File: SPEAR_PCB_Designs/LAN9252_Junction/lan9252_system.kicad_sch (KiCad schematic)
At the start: 32 parts, among them SW2 SW_MEC_5E, U1 LAN9252_ML, Y1 25MHz

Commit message: Almost finished board
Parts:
- removed C1, C3: 1uF, Capacitor_SMD:C_0201_0603Metric, symbol Device:C
- removed C11, C22, C8: 0.1uF, Capacitor_SMD:C_0201_0603Metric, symbol Device:C
- removed R2: 10k, Resistor_SMD:R_0603_1608Metric, symbol Device:R_US
- added C66: 0.1uF, Capacitor_SMD:C_0201_0603Metric, symbol Device:C
- added R5, R6: 141 R, Resistor_SMD:R_0402_1005Metric, symbol Device:R_US
- added R57: 10k, Resistor_SMD:R_0402_1005Metric, symbol Device:R_US
- C1: renamed from C6; footprint Capacitor_SMD:C_0201_0603Metric -> Capacitor_SMD:C_0402_1005Metric
- C10: renamed from C20; value 0.1uF -> 470 pF; footprint Capacitor_SMD:C_0201_0603Metric -> Capacitor_SMD:C_0402_1005Metric
- C11: renamed from C12; footprint Capacitor_SMD:C_0201_0603Metric -> Capacitor_SMD:C_0402_1005Metric
- C12: renamed from C21; footprint Capacitor_SMD:C_0201_0603Metric -> Capacitor_SMD:C_0402_1005Metric
- C13, C14, C15, C16, C17, C2, C5: footprint Capacitor_SMD:C_0201_0603Metric -> Capacitor_SMD:C_0402_1005Metric
- C3: renamed from C4; footprint Capacitor_SMD:C_0201_0603Metric -> Capacitor_SMD:C_0402_1005Metric
- C4: renamed from C7; footprint Capacitor_SMD:C_0201_0603Metric -> Capacitor_SMD:C_0402_1005Metric
- C6: renamed from C9; footprint Capacitor_SMD:C_0201_0603Metric -> Capacitor_SMD:C_0402_1005Metric
- C7: renamed from C18; value 0.1uF -> 1uF; footprint Capacitor_SMD:C_0201_0603Metric -> Capacitor_SMD:C_0402_1005Metric
- C8: renamed from C10; footprint Capacitor_SMD:C_0201_0603Metric -> Capacitor_SMD:C_0402_1005Metric
- C9: renamed from C19; footprint Capacitor_SMD:C_0201_0603Metric -> Capacitor_SMD:C_0402_1005Metric
- FB1, FB2, FB3, FB4: footprint Footprints SPEAR:Ferrite_bead -> SPEAR_FOOTPRINTS:Ferrite_bead
- R3: renamed from R25; footprint Resistor_SMD:R_0603_1608Metric -> Resistor_SMD:R_0402_1005Metric
- R4: renamed from R1; footprint Resistor_SMD:R_0603_1608Metric -> Resistor_SMD:R_0402_1005Metric
- U1: footprint Footprints SPEAR:QFP50P1200X1200X120-65N -> SPEAR_FOOTPRINTS:LAN9252_QFN UPDATED
- Y1: footprint Crystal:Crystal_HC50_Vertical -> SPEAR_FOOTPRINTS:Y_Wurth_WE-XTAL_Quartz-HC49-4HSMX
- renumbered SW2 to SW1
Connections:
- net GNDREF is gone; now on net GND: C1.1, C10.2, C11.2, C12.2, C13.2, C14.2, C15.2, C16.2, C17.2, C4.1, C6.2, C7.2, C8.2, C9.2, R4.1, SW1.1, SW1.2, U1.4 (OSCVSS), U1.41 (TESTMODE), U1.65 (VSS), U1.8 (~{FXLOSEN}), U1.9 (FXSDA/FXLOSA/~{FXSDENA})
- net +3.3V: now also R57.1; no longer C5.1
- net GND: now also C2.2, C3.2, U1.10 (FXSDB/FXLOSB/~{FXSDENB}), C66.2, R5.2, R6.2
- net MII_TXD2: now also R5.1
- net MII_TXD3: now also R6.1
- net at FB3.1, U1.58 (VDD33BIAS): now also C5.1
- net TP3 renamed TP1
- net TP1: now also C66.1, R57.2
- no-connect marks 11 -> 10
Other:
- note added: "TX SHIFT STRAP"
- moved on the sheet: C4, C5, FB3, SW1

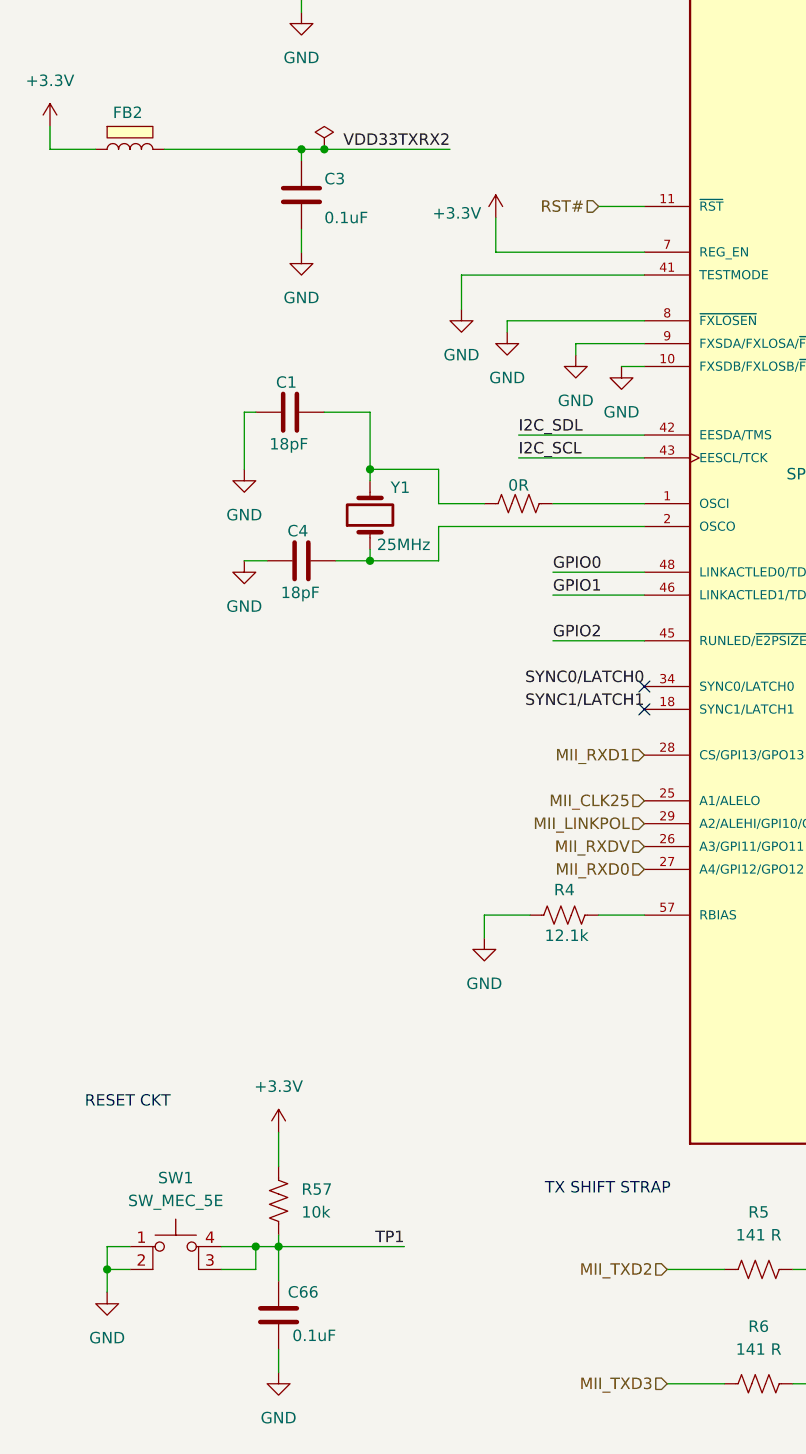
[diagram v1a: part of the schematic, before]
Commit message: Updated Junction board
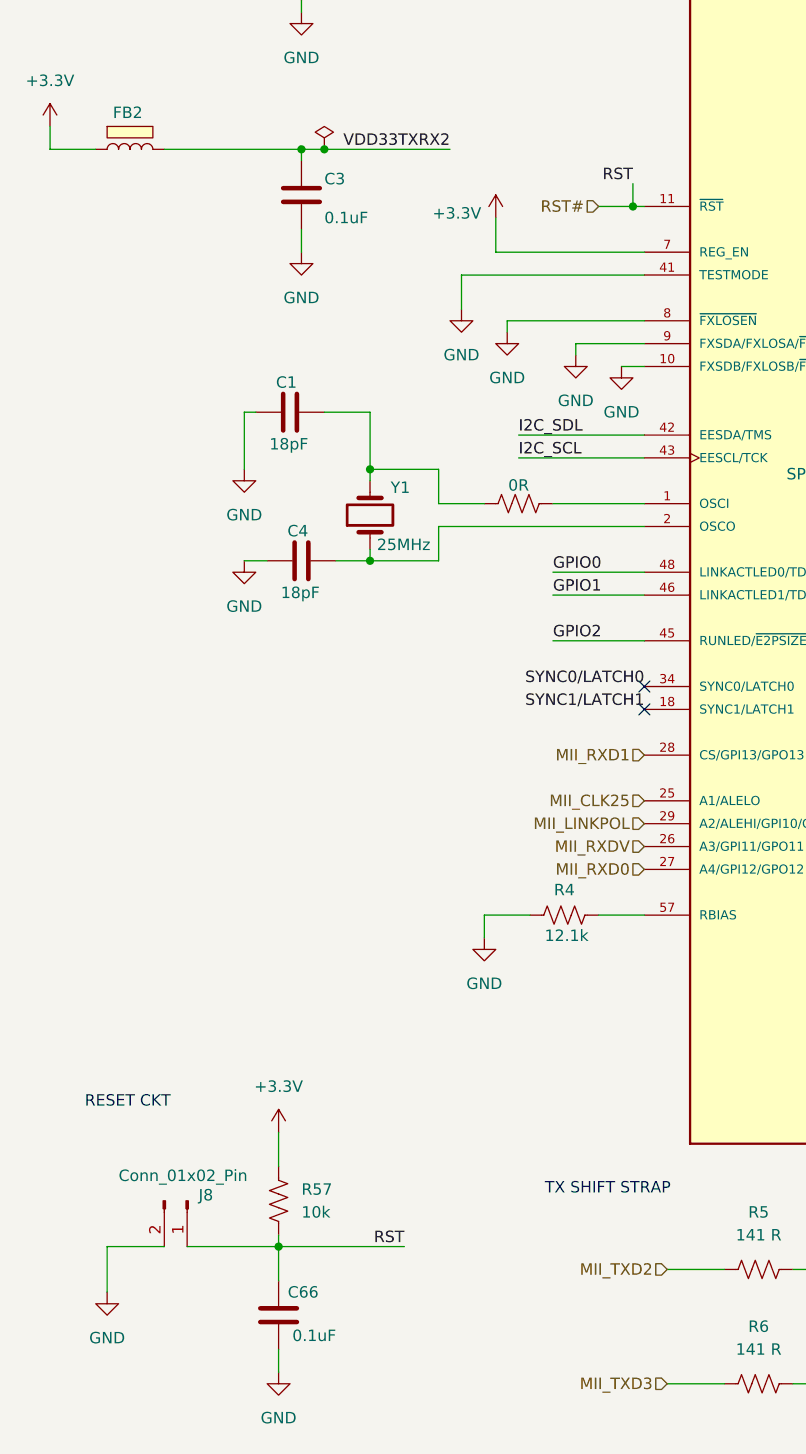
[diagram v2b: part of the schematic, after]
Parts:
- removed SW1: SW_MEC_5E, Button_Switch_THT:SW_PUSH_6mm, symbol Switch:SW_MEC_5E
- added J8: Conn_01x02_Pin, TestPoint:TestPoint_2Pads_Pitch2.54mm_Drill0.8mm, symbol Connector:Conn_01x02_Pin
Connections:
- net TP1 is gone; now on net RST#: C66.1, R57.2
- net GND: now also J8.2 (Pin_2)
- net RST#: now also J8.1 (Pin_1)
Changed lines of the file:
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@@
 	)
 	(junction
+		(at 83.82 55.88)
+		(diameter 0)
+		(color 0 0 0 0)
+	)
+	(junction
 		(at 160.02 35.56)
 		(diameter 0)
@@
 	)
 	(junction
-		(at 25.4 173.99)
-		(diameter 0)
-		(color 0 0 0 0)
-	)
-	(junction
 		(at 237.49 104.14)
 		(diameter 0)
@@
 	)
 	(junction
-		(at 41.91 171.45)
-		(diameter 0)
-		(color 0 0 0 0)
-	)
-	(junction
 		(at 223.52 72.39)
 		(diameter 0)
@@
 	(wire
 		(pts
+			(xy 83.82 53.34) (xy 83.82 55.88)
+		)
+		(stroke
+			(width 0)
+			(type default)
+		)
+	)
+	(wire
+		(pts
 			(xy 237.49 99.06) (xy 237.49 104.14)
 		)
@@
 	(wire
 		(pts
+			(xy 34.29 171.45) (xy 44.45 171.45)
+		)
+		(stroke
+			(width 0)
+			(type default)
+		)
+	)
+	(wire
+		(pts
 			(xy 62.23 88.9) (xy 62.23 85.09)
 		)
@@
 	(wire
 		(pts
-			(xy 27.94 173.99) (xy 25.4 173.99)
-		)
-		(stroke
-			(width 0)
-			(type default)
-		)
-	)
-	(wire
-		(pts
 			(xy 40.64 78.74) (xy 41.91 78.74)
 		)
@@
 	(wire
 		(pts
-			(xy 160.02 43.18) (xy 156.21 43.18)
+			(xy 83.82 55.88) (xy 85.09 55.88)
 		)
 		(stroke
@@
 	(wire
 		(pts
-			(xy 49.53 24.13) (xy 63.5 24.13)
+			(xy 160.02 43.18) (xy 156.21 43.18)
 		)
 		(stroke
@@
 	(wire
 		(pts
-			(xy 25.4 173.99) (xy 25.4 176.53)
+			(xy 49.53 24.13) (xy 63.5 24.13)
 		)
 		(stroke
@@
 	(wire
 		(pts
-			(xy 25.4 173.99) (xy 25.4 171.45)
+			(xy 25.4 171.45) (xy 25.4 176.53)
 		)
 		(stroke
@@
 	(wire
 		(pts
-			(xy 27.94 171.45) (xy 25.4 171.45)
+			(xy 25.4 171.45) (xy 31.75 171.45)
 		)
 		(stroke
@@
 	(wire
 		(pts
-			(xy 41.91 171.45) (xy 44.45 171.45)
-		)
-		(stroke
-			(width 0)
-			(type default)
-		)
-	)
-	(wire
-		(pts
-			(xy 80.01 55.88) (xy 85.09 55.88)
+			(xy 80.01 55.88) (xy 83.82 55.88)
 		)
 		(stroke
@@
 	(wire
 		(pts
-			(xy 41.91 173.99) (xy 41.91 171.45)
-		)
-		(stroke
-			(width 0)
-			(type default)
-		)
-	)
-	(wire
-		(pts
-			(xy 38.1 171.45) (xy 41.91 171.45)
-		)
-		(stroke
-			(width 0)
-			(type default)
-		)
-	)
-	(wire
-		(pts
 			(xy 156.21 78.74) (xy 166.37 78.74)
 		)
@@
 	(wire
 		(pts
-			(xy 38.1 173.99) (xy 41.91 173.99)
-		)
-		(stroke
-			(width 0)
-			(type default)
-		)
-	)
-	(wire
-		(pts
 			(xy 213.36 142.24) (xy 226.06 142.24)
 		)
@@
 		)
 	)
-	(label "TP1"
+	(label "RST"
 		(at 58.42 171.45 180)
 		(effects
@@
 		)
 	)
+	(label "RST"
+		(at 83.82 53.34 180)
+		(effects
+			(font
+				(size 1.27 1.27)
+			)
+			(justify right bottom)
+		)
+	)
 	(label "VDDCR"
 		(at 162.56 43.18 180)
@@
 	)
 	(symbol
+		(lib_id "Connector:Conn_01x02_Pin")
+		(at 34.29 166.37 270)
+		(unit 1)
+		(exclude_from_sim no)
+		(in_bom yes)
+		(on_board yes)
+		(dnp no)
+		(property "Reference" "J8"
+			(at 35.56 165.7349 90)
+			(effects
+				(font
+					(size 1.27 1.27)
+				)
+				(justify left)
+			)
+		)
+		(property "Value" "Conn_01x02_Pin"
+			(at 26.67 163.576 90)
+			(effects
+				(font
+					(size 1.27 1.27)
+				)
+				(justify left)
+			)
+		)
+		(property "Footprint" "TestPoint:TestPoint_2Pads_Pitch2.54mm_Drill0.8mm"
+			(at 34.29 166.37 0)
+			(effects
+				(font
+					(size 1.27 1.27)
+				)
+				(hide yes)
+			)
+		)
+		(property "Datasheet" "~"
+			(at 34.29 166.37 0)
+			(effects
+				(font
+					(size 1.27 1.27)
+				)
+				(hide yes)
+			)
+		)
+		(property "Description" "Generic connector, single row, 01x02, script generated"
+			(at 34.29 166.37 0)
+			(effects
+				(font
+					(size 1.27 1.27)
+				)
+				(hide yes)
+			)
+		)
+		(pin "1"
+		)
+		(pin "2"
+		)
+		(instances
+			(project ""
+				(path "/16d72164-3a84-4f74-a868-383d0ad57128/51ada2c8-3854-4465-9d64-3e8aa0c5daf2"
+					(reference "J8")
+					(unit 1)
+				)
+				(path "/16d72164-3a84-4f74-a868-383d0ad57128/52e6a653-4436-4d7a-ae83-cfeea5b0a028"
+					(reference "J9")
+					(unit 1)
+				)
+			)
+		)
+	)
+	(symbol
 		(lib_id "Device:FerriteBead")
 		(at 241.3 21.59 0)
@@
 					(unit 1)
 				)
-			)
-		)
-	)
-	(symbol
-		(lib_id "Switch:SW_MEC_5E")
-		(at 33.02 173.99 0)
-		(unit 1)
-		(exclude_from_sim no)
-		(in_bom yes)
-		(on_board yes)
-		(dnp no)
-		(fields_autoplaced yes)
-		(property "Reference" "SW1"
-			(at 33.02 163.83 0)
-			(effects
-				(font
-					(size 1.27 1.27)
-				)
-			)
-		)
-		(property "Value" "SW_MEC_5E"
-			(at 33.02 166.37 0)
-			(effects
-				(font
-					(size 1.27 1.27)
-				)
-			)
-		)
-		(property "Footprint" "Button_Switch_THT:SW_PUSH_6mm"
-			(at 33.02 166.37 0)
-			(effects
-				(font
-					(size 1.27 1.27)
-				)
-				(hide yes)
-			)
-		)
-		(property "Datasheet" "http://www.apem.com/int/index.php?controller=attachment&id_attachment=1371"
-			(at 33.02 166.37 0)
-			(effects
-				(font
-					(size 1.27 1.27)
-				)
-				(hide yes)
-			)
-		)
-		(property "Description" "MEC 5E single pole normally-open tactile switch"
-			(at 33.02 173.99 0)
-			(effects
-				(font
-					(size 1.27 1.27)
-				)
-				(hide yes)
-			)
-		)
-		(pin "1"
-		)
-		(pin "3"
-		)
-		(pin "4"
-		)
-		(pin "2"
-		)
-		(instances
-			(project "LAN9252_Junction"
-				(path "/16d72164-3a84-4f74-a868-383d0ad57128/51ada2c8-3854-4465-9d64-3e8aa0c5daf2"
-					(reference "SW1")
-					(unit 1)
-				)
-				(path "/16d72164-3a84-4f74-a868-383d0ad57128/52e6a653-4436-4d7a-ae83-cfeea5b0a028"
-					(reference "SW2")
-					(unit 1)
-				)
